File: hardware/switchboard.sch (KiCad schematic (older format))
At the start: 0 parts

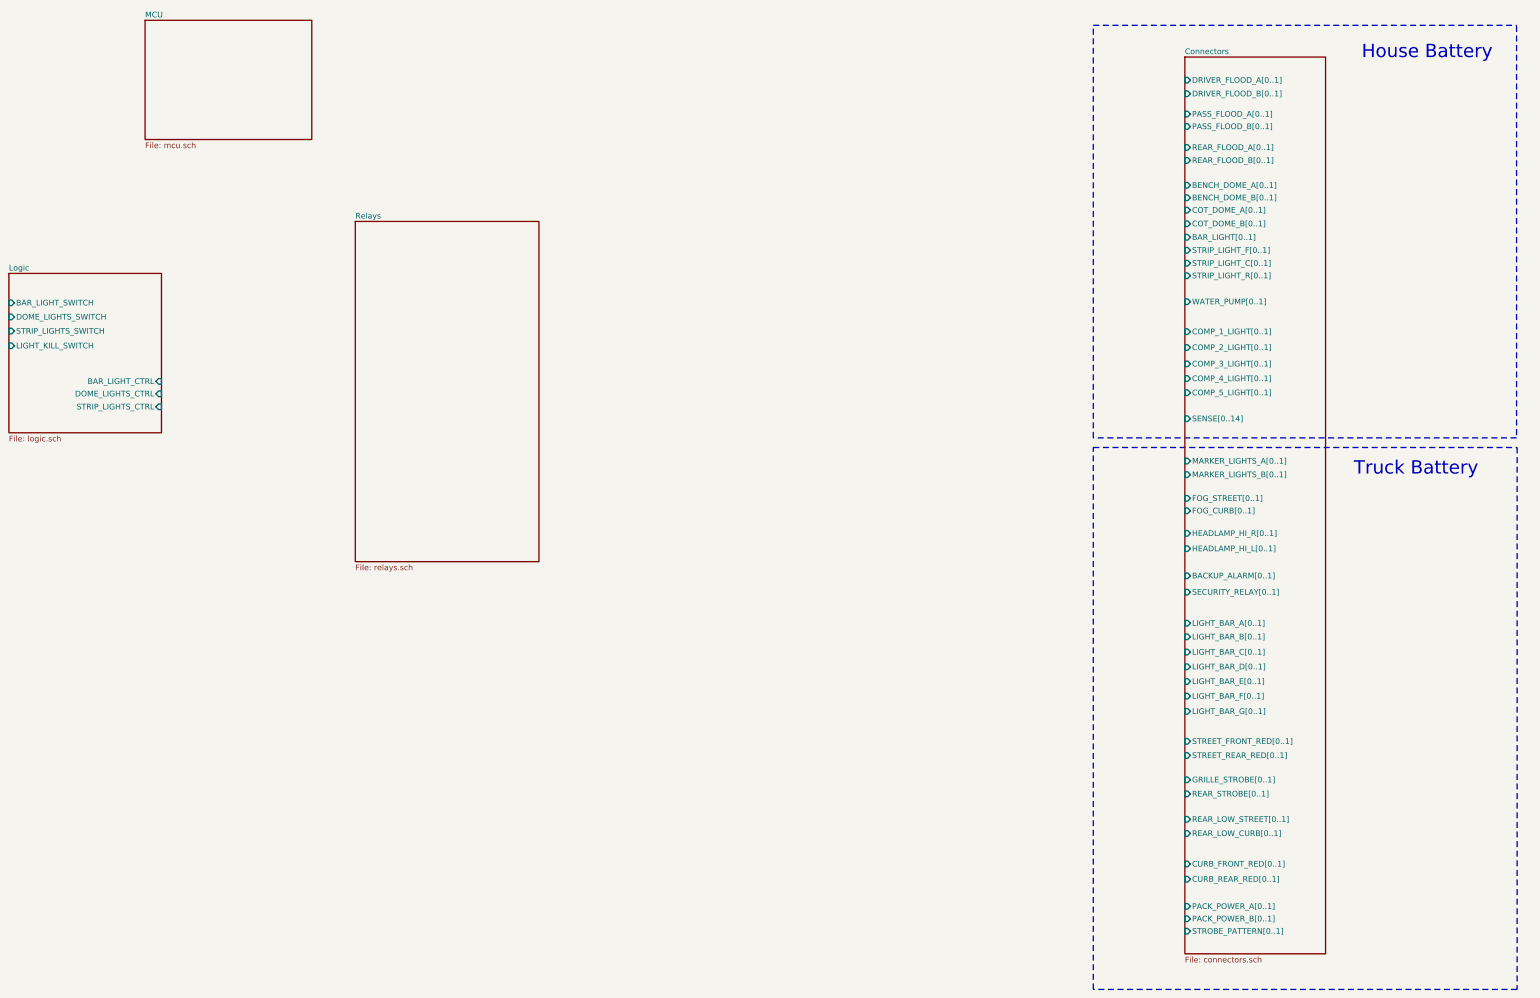
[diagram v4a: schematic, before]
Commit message: hardware: migrate to VN750 instead of relays
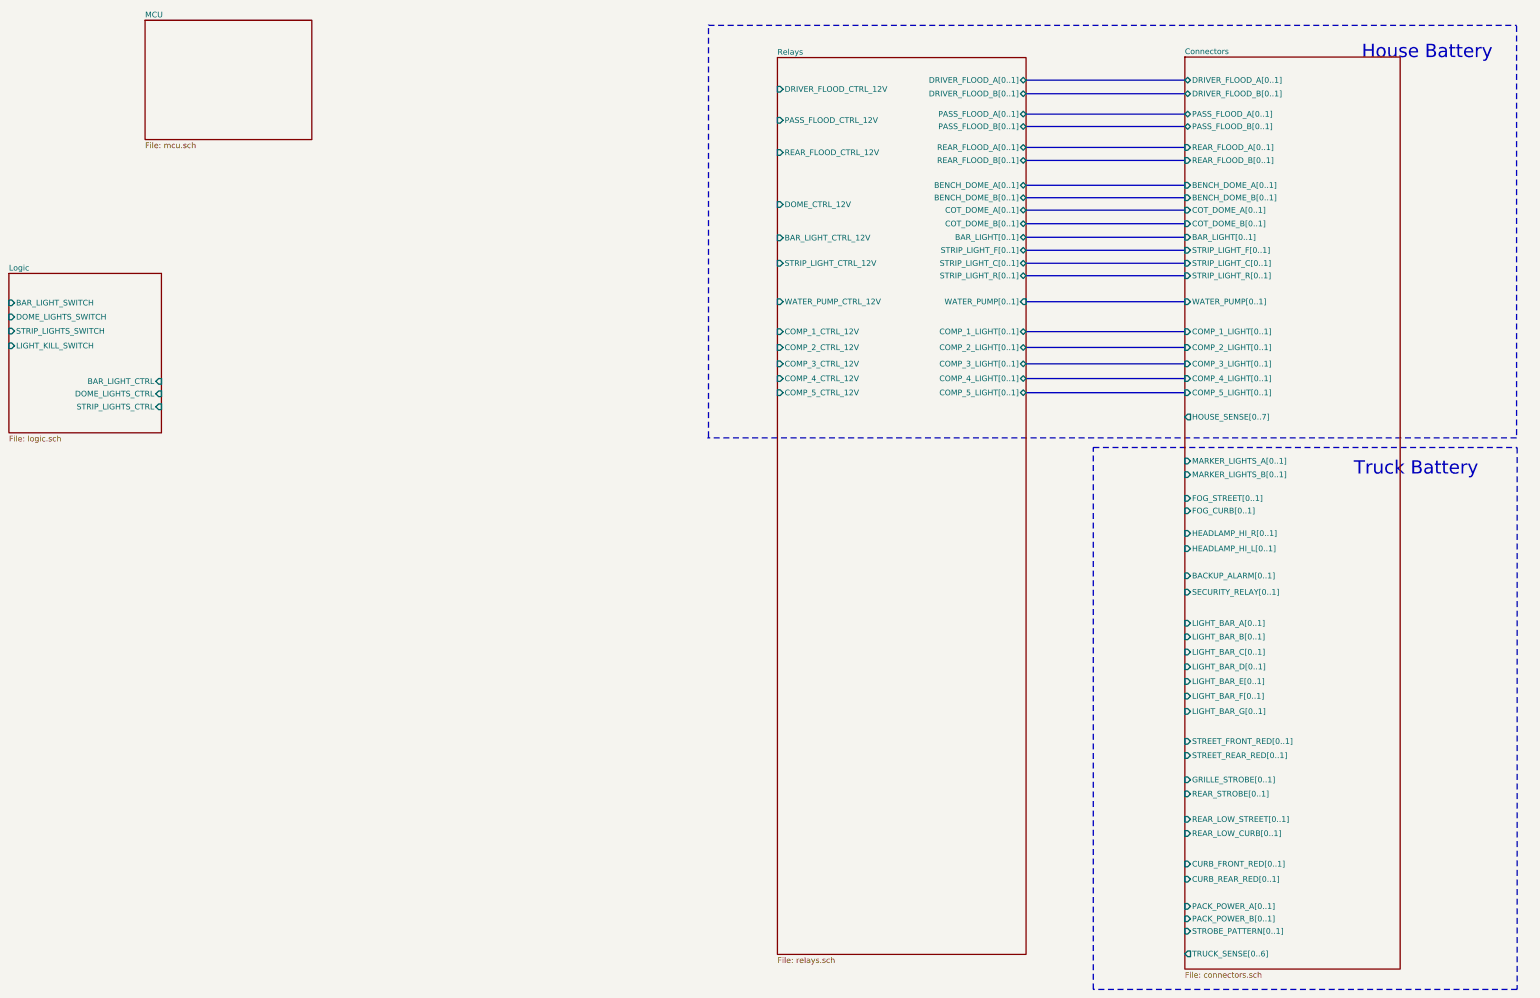
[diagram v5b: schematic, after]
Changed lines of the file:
@@
 $EndSheet
 $Sheet
-S 5085 2640 1625 3010
+S 8820 1190 2200 7935
 U 605C1303
 F0 "Relays" 50
 F1 "relays.sch" 50
+F2 "DRIVER_FLOOD_A[0..1]" B R 11020 1390 50
+F3 "DRIVER_FLOOD_CTRL_12V" I L 8820 1470 50
+F4 "DRIVER_FLOOD_B[0..1]" B R 11020 1510 50
+F5 "PASS_FLOOD_A[0..1]" B R 11020 1690 50
+F6 "PASS_FLOOD_CTRL_12V" I L 8820 1745 50
+F7 "PASS_FLOOD_B[0..1]" B R 11020 1800 50
+F8 "REAR_FLOOD_A[0..1]" B R 11020 1985 50
+F9 "REAR_FLOOD_CTRL_12V" I L 8820 2030 50
+F10 "REAR_FLOOD_B[0..1]" B R 11020 2100 50
+F11 "BENCH_DOME_A[0..1]" B R 11020 2320 50
+F12 "DOME_CTRL_12V" I L 8820 2490 50
+F13 "BENCH_DOME_B[0..1]" B R 11020 2430 50
+F14 "COT_DOME_A[0..1]" B R 11020 2540 50
+F15 "COT_DOME_B[0..1]" B R 11020 2660 50
+F16 "BAR_LIGHT[0..1]" B R 11020 2780 50
+F17 "BAR_LIGHT_CTRL_12V" I L 8820 2785 50
+F18 "STRIP_LIGHT_F[0..1]" B R 11020 2895 50
+F19 "STRIP_LIGHT_CTRL_12V" I L 8820 3010 50
+F20 "STRIP_LIGHT_C[0..1]" B R 11020 3010 50
+F21 "STRIP_LIGHT_R[0..1]" B R 11020 3120 50
+F22 "COMP_1_LIGHT[0..1]" B R 11020 3615 50
+F23 "COMP_1_CTRL_12V" I L 8820 3615 50
+F24 "COMP_2_LIGHT[0..1]" B R 11020 3755 50
+F25 "COMP_2_CTRL_12V" I L 8820 3755 50
+F26 "COMP_3_LIGHT[0..1]" B R 11020 3900 50
+F27 "COMP_3_CTRL_12V" I L 8820 3900 50
+F28 "COMP_4_LIGHT[0..1]" B R 11020 4030 50
+F29 "COMP_4_CTRL_12V" I L 8820 4030 50
+F30 "COMP_5_LIGHT[0..1]" B R 11020 4155 50
+F31 "COMP_5_CTRL_12V" I L 8820 4155 50
+F32 "WATER_PUMP[0..1]" I R 11020 3350 50
+F33 "WATER_PUMP_CTRL_12V" I L 8820 3350 50
 $EndSheet
 $Sheet
-S 12425 1185 1245 7935
+S 12425 1185 1905 8070
 U 605C149A
 F0 "Connectors" 50
 F1 "connectors.sch" 50
-F2 "DRIVER_FLOOD_A[0..1]" I L 12425 1390 50
+F2 "DRIVER_FLOOD_A[0..1]" B L 12425 1390 50
 F3 "STROBE_PATTERN[0..1]" I L 12425 8920 50
 F4 "BACKUP_ALARM[0..1]" I L 12425 5775 50
@@
 F7 "FOG_CURB[0..1]" I L 12425 5200 50
 F8 "FOG_STREET[0..1]" I L 12425 5090 50
-F9 "PASS_FLOOD_A[0..1]" I L 12425 1690 50
+F9 "PASS_FLOOD_A[0..1]" B L 12425 1690 50
 F10 "REAR_FLOOD_A[0..1]" I L 12425 1985 50
 F11 "BENCH_DOME_A[0..1]" I L 12425 2320 50
@@
 F22 "COMP_2_LIGHT[0..1]" I L 12425 3755 50
 F23 "COMP_1_LIGHT[0..1]" I L 12425 3615 50
-F24 "SENSE[0..14]" I L 12425 4385 50
-F25 "LIGHT_BAR_F[0..1]" I L 12425 6840 50
-F26 "LIGHT_BAR_E[0..1]" I L 12425 6710 50
-F27 "LIGHT_BAR_D[0..1]" I L 12425 6580 50
-F28 "LIGHT_BAR_C[0..1]" I L 12425 6450 50
-F29 "LIGHT_BAR_B[0..1]" I L 12425 6315 50
-F30 "STREET_REAR_RED[0..1]" I L 12425 7365 50
-F31 "STREET_FRONT_RED[0..1]" I L 12425 7240 50
-F32 "GRILLE_STROBE[0..1]" I L 12425 7580 50
-F33 "REAR_STROBE[0..1]" I L 12425 7705 50
-F34 "REAR_LOW_CURB[0..1]" I L 12425 8055 50
-F35 "REAR_LOW_STREET[0..1]" I L 12425 7930 50
-F36 "PACK_POWER_A[0..1]" I L 12425 8700 50
-F37 "PACK_POWER_B[0..1]" I L 12425 8810 50
-F38 "CURB_REAR_RED[0..1]" I L 12425 8460 50
-F39 "CURB_FRONT_RED[0..1]" I L 12425 8325 50
-F40 "LIGHT_BAR_G[0..1]" I L 12425 6975 50
-F41 "LIGHT_BAR_A[0..1]" I L 12425 6195 50
-F42 "MARKER_LIGHTS_B[0..1]" I L 12425 4880 50
-F43 "DRIVER_FLOOD_B[0..1]" I L 12425 1510 50
-F44 "PASS_FLOOD_B[0..1]" I L 12425 1800 50
-F45 "REAR_FLOOD_B[0..1]" I L 12425 2100 50
-F46 "BENCH_DOME_B[0..1]" I L 12425 2430 50
-F47 "COT_DOME_B[0..1]" I L 12425 2660 50
-F48 "STRIP_LIGHT_R[0..1]" I L 12425 3120 50
+F24 "LIGHT_BAR_F[0..1]" I L 12425 6840 50
+F25 "LIGHT_BAR_E[0..1]" I L 12425 6710 50
+F26 "LIGHT_BAR_D[0..1]" I L 12425 6580 50
+F27 "LIGHT_BAR_C[0..1]" I L 12425 6450 50
+F28 "LIGHT_BAR_B[0..1]" I L 12425 6315 50
+F29 "STREET_REAR_RED[0..1]" I L 12425 7365 50
+F30 "STREET_FRONT_RED[0..1]" I L 12425 7240 50
+F31 "GRILLE_STROBE[0..1]" I L 12425 7580 50
+F32 "REAR_STROBE[0..1]" I L 12425 7705 50
+F33 "REAR_LOW_CURB[0..1]" I L 12425 8055 50
+F34 "REAR_LOW_STREET[0..1]" I L 12425 7930 50
+F35 "PACK_POWER_A[0..1]" I L 12425 8700 50
+F36 "PACK_POWER_B[0..1]" I L 12425 8810 50
+F37 "CURB_REAR_RED[0..1]" I L 12425 8460 50
+F38 "CURB_FRONT_RED[0..1]" I L 12425 8325 50
+F39 "LIGHT_BAR_G[0..1]" I L 12425 6975 50
+F40 "LIGHT_BAR_A[0..1]" I L 12425 6195 50
+F41 "MARKER_LIGHTS_B[0..1]" I L 12425 4880 50
+F42 "DRIVER_FLOOD_B[0..1]" B L 12425 1510 50
+F43 "PASS_FLOOD_B[0..1]" B L 12425 1800 50
+F44 "REAR_FLOOD_B[0..1]" I L 12425 2100 50
+F45 "BENCH_DOME_B[0..1]" I L 12425 2430 50
+F46 "COT_DOME_B[0..1]" I L 12425 2660 50
+F47 "STRIP_LIGHT_R[0..1]" I L 12425 3120 50
+F48 "HOUSE_SENSE[0..7]" O L 12425 4370 50
+F49 "TRUCK_SENSE[0..6]" O L 12425 9120 50
 $EndSheet
 Wire Notes Line
-	15360 4555 11615 4555
+	15360 4555 8200 4555
 Wire Notes Line
-	11615 4555 11615 905
+	8210 4550 8210 895
 Wire Notes Line
-	11615 905  15360 905
+	8210 905  15360 905
 Wire Notes Line
 	15360 910  15360 4560
@@
 Wire Notes Line
 	15365 9435 11615 9435
+Text Notes 13920 4895 0    118  ~ 0
+Truck Battery
 Wire Notes Line
 	11615 9435 11615 4640
-Text Notes 13920 4895 0    118  ~ 0
-Truck Battery
+Wire Bus Line
+	11020 1390 12425 1390
+Wire Bus Line
+	12425 1510 11020 1510
+Wire Bus Line
+	11020 1690 12425 1690
+Wire Bus Line
+	12425 1800 11020 1800
+Wire Bus Line
+	11020 1985 12425 1985
+Wire Bus Line
+	12425 2100 11020 2100
+Wire Bus Line
+	11020 2320 12425 2320
+Wire Bus Line
+	12425 2430 11020 2430
+Wire Bus Line
+	11020 2540 12425 2540
+Wire Bus Line
+	12425 2660 11020 2660
+Wire Bus Line
+	11020 2780 12425 2780
+Wire Bus Line
+	12425 2895 11020 2895
+Wire Bus Line
+	12425 3010 11020 3010
+Wire Bus Line
+	11020 3120 12425 3120
+Wire Bus Line
+	12425 3350 11020 3350
+Wire Bus Line
+	11020 3615 12425 3615
+Wire Bus Line
+	12425 3755 11020 3755
+Wire Bus Line
+	11020 3900 12425 3900
+Wire Bus Line
+	12425 4030 11020 4030
+Wire Bus Line
+	11020 4155 12425 4155
 $EndSCHEMATC
